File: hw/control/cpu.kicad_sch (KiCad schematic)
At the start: 33 parts, among them J301 Conn_02x05_Odd_Even, J302 Conn_01x04, J303 Raspberry_Pi_0_2_3, J304 Conn_01x07, J305 Micro_SD_Card, J306 Conn_01x06, Q301 SI2312CDS-T1-GE3, SW301 SW_Push, U301 CAT24C256

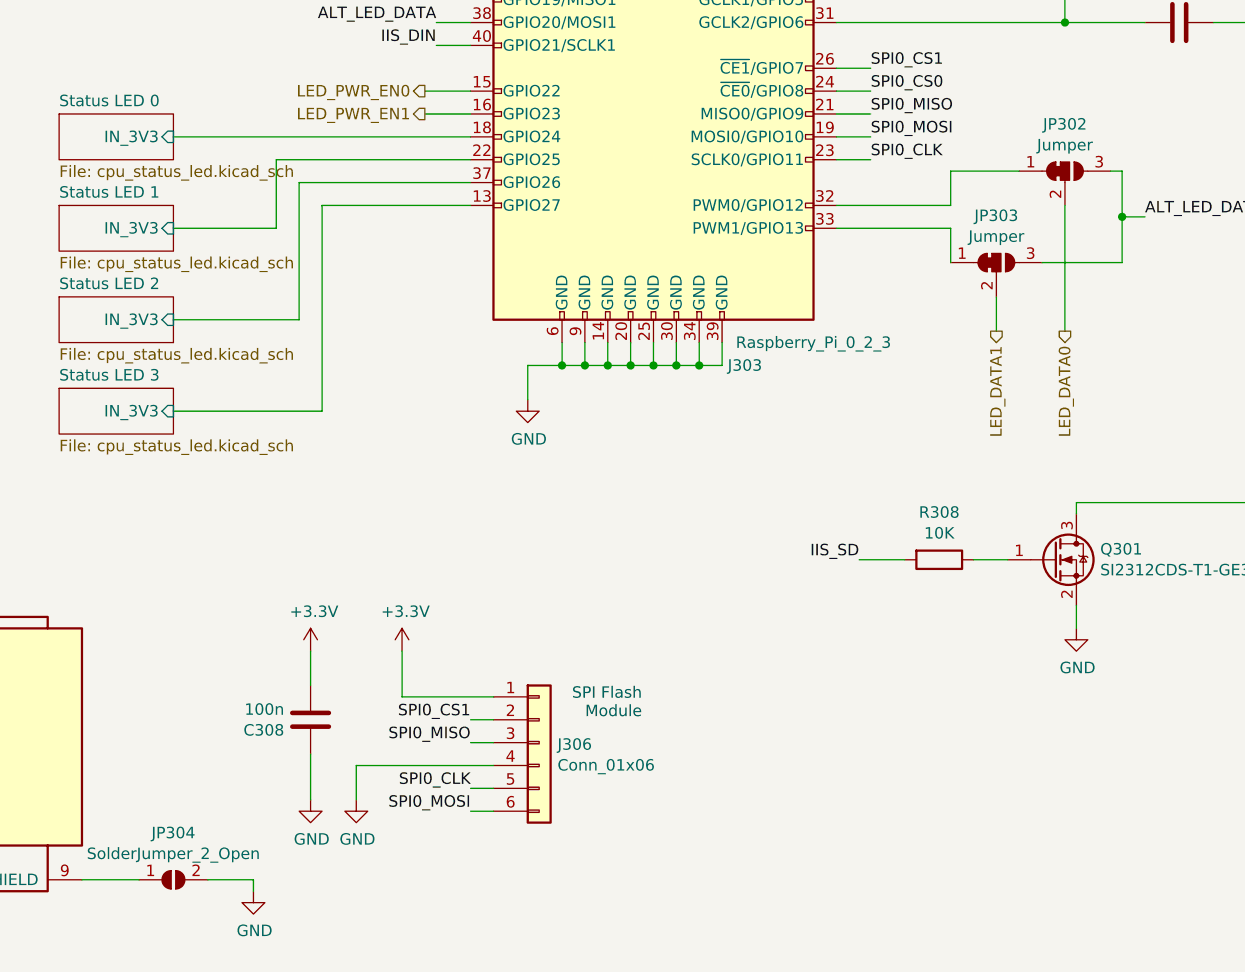
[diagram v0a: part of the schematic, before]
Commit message: [hw] Update to KiCAD 7
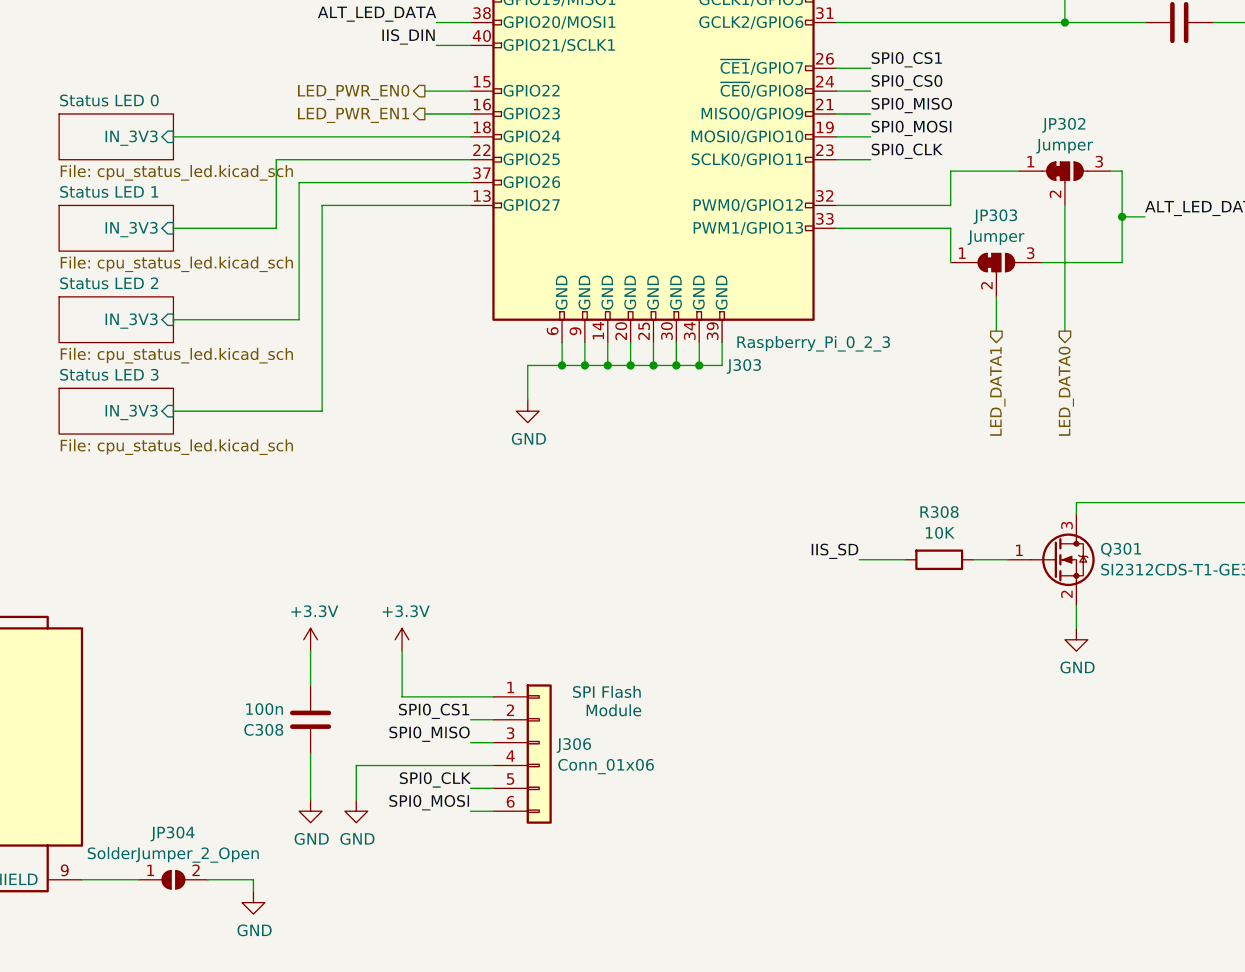
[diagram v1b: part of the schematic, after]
